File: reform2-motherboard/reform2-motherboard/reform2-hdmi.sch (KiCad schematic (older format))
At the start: 12 parts, among them J4 HDMI_A

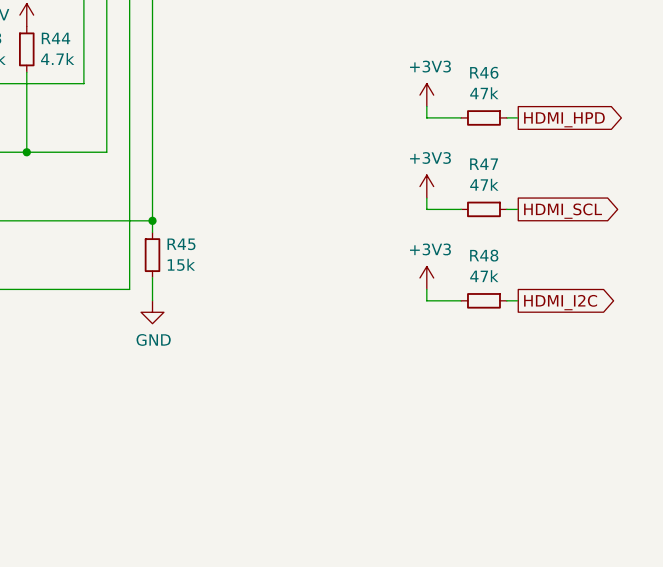
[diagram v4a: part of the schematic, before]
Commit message: WIP: reform2 motherboard: more schematics tuning, preliminary selection of most components
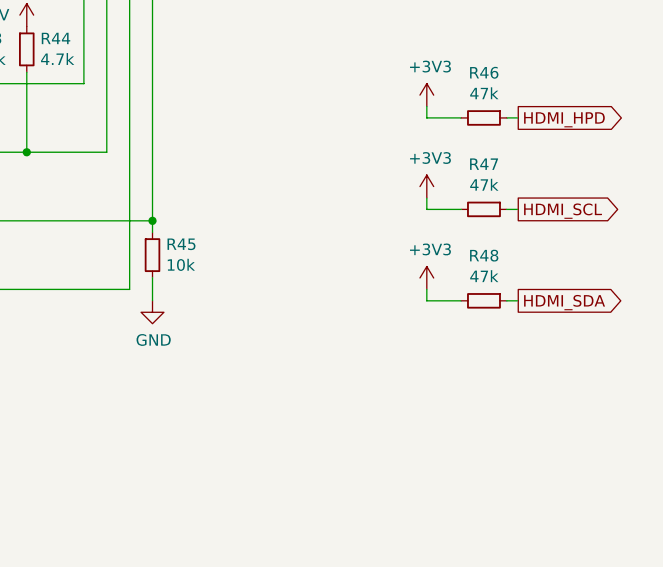
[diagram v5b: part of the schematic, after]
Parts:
- C27, C28, C29, C30: Manufacturer (none) -> TDK; Manufacturer_No (none) -> CGA3E2X8R1E104K080AE
- J4: Manufacturer (none) -> Wurth; Manufacturer_No (none) -> 685119134923
- R43, R44: Manufacturer (none) -> Yageo; Manufacturer_No (none) -> RC0603FR-074K7L
- R45: value 15k -> 10k; Manufacturer (none) -> Vishay Dale; Manufacturer_No (none) -> CRCW060310K0JNEAC
- R46, R47, R48: Manufacturer (none) -> Vishay Dale; Manufacturer_No (none) -> CRCW060347K0FKEAC
- U?1: Manufacturer (none) -> Texas Instruments; Manufacturer_No (none) -> CM2020-00TR
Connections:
- net HDMI_I2C is gone; now on net HDMI_SDA: R48.1
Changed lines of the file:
@@
 F 2 "footprints:HDMI-685119134923" H 8075 2600 50  0001 C CNN
 F 3 "https://en.wikipedia.org/wiki/HDMI" H 8075 2600 50  0001 C CNN
+F 4 "Wurth" H 8050 2600 50  0001 C CNN "Manufacturer"
+F 5 "685119134923" H 8050 2600 50  0001 C CNN "Manufacturer_No"
 	1    8050 2600
 	1    0    0    -1
@@
 F 4 "CM2020-00TR Series 10.8 V HDMI Transmitter Port Protection and Interface Device" H 3350 3150 50  0001 L BNN "Field6"
 F 5 "ON Semiconductor" H 4450 3050 50  0001 L BNN "Field8"
+F 6 "Texas Instruments" H 4800 5100 50  0001 C CNN "Manufacturer"
+F 7 "CM2020-00TR" H 4800 5100 50  0001 C CNN "Manufacturer_No"
 	1    4800 5100
 	1    0    0    -1
@@
 P 7550 5550
 F 0 "R45" H 7609 5596 50  0000 L CNN
-F 1 "15k" H 7609 5505 50  0000 L CNN
+F 1 "10k" H 7609 5505 50  0000 L CNN
 F 2 "Resistor_SMD:R_0603_1608Metric" H 7550 5550 50  0001 C CNN
 F 3 "~" H 7550 5550 50  0001 C CNN
+F 4 "Vishay Dale" H 7550 5550 50  0001 C CNN "Manufacturer"
+F 5 "CRCW060310K0JNEAC" H 7550 5550 50  0001 C CNN "Manufacturer_No"
 	1    7550 5550
 	1    0    0    -1
@@
 F 2 "Capacitor_SMD:C_0603_1608Metric" H 7400 1400 50  0001 C CNN
 F 3 "~" H 7400 1400 50  0001 C CNN
+F 4 "TDK" H 7400 1400 50  0001 C CNN "Manufacturer"
+F 5 "CGA3E2X8R1E104K080AE" H 7400 1400 50  0001 C CNN "Manufacturer_No"
 	1    7400 1400
 	1    0    0    -1
@@
 F 2 "Resistor_SMD:R_0603_1608Metric" H 6700 4650 50  0001 C CNN
 F 3 "~" H 6700 4650 50  0001 C CNN
+F 4 "Yageo" H 6700 4650 50  0001 C CNN "Manufacturer"
+F 5 "RC0603FR-074K7L" H 6700 4650 50  0001 C CNN "Manufacturer_No"
 	1    6700 4650
 	1    0    0    -1
@@
 F 2 "Resistor_SMD:R_0603_1608Metric" H 7000 4650 50  0001 C CNN
 F 3 "~" H 7000 4650 50  0001 C CNN
+F 4 "Yageo" H 7000 4650 50  0001 C CNN "Manufacturer"
+F 5 "RC0603FR-074K7L" H 7000 4650 50  0001 C CNN "Manufacturer_No"
 	1    7000 4650
 	1    0    0    -1
@@
 F 2 "Capacitor_SMD:C_0603_1608Metric" H 6800 4100 50  0001 C CNN
 F 3 "~" H 6800 4100 50  0001 C CNN
+F 4 "TDK" H 6800 4100 50  0001 C CNN "Manufacturer"
+F 5 "CGA3E2X8R1E104K080AE" H 6800 4100 50  0001 C CNN "Manufacturer_No"
 	1    6800 4100
 	0    -1   -1   0
@@
 F 2 "Capacitor_SMD:C_0603_1608Metric" H 6200 4000 50  0001 C CNN
 F 3 "~" H 6200 4000 50  0001 C CNN
+F 4 "TDK" H 6200 4000 50  0001 C CNN "Manufacturer"
+F 5 "CGA3E2X8R1E104K080AE" H 6200 4000 50  0001 C CNN "Manufacturer_No"
 	1    6200 4000
 	0    1    1    0
@@
 F 2 "Resistor_SMD:R_0603_1608Metric" H 9000 4950 50  0001 C CNN
 F 3 "~" H 9000 4950 50  0001 C CNN
+F 4 "Vishay Dale" H 9000 4950 50  0001 C CNN "Manufacturer"
+F 5 "CRCW060347K0FKEAC" H 9000 4950 50  0001 C CNN "Manufacturer_No"
 	1    9000 4950
 	0    1    1    0
@@
 F 2 "Capacitor_SMD:C_0603_1608Metric" H 6000 4500 50  0001 C CNN
 F 3 "~" H 6000 4500 50  0001 C CNN
+F 4 "TDK" H 6000 4500 50  0001 C CNN "Manufacturer"
+F 5 "CGA3E2X8R1E104K080AE" H 6000 4500 50  0001 C CNN "Manufacturer_No"
 	1    6000 4500
 	0    1    1    0
@@
 F 2 "Resistor_SMD:R_0603_1608Metric" H 9000 5350 50  0001 C CNN
 F 3 "~" H 9000 5350 50  0001 C CNN
+F 4 "Vishay Dale" H 9000 5350 50  0001 C CNN "Manufacturer"
+F 5 "CRCW060347K0FKEAC" H 9000 5350 50  0001 C CNN "Manufacturer_No"
 	1    9000 5350
 	0    1    1    0
@@
 	8750 5350 8750 5300
 Text GLabel 9150 5750 2    50   Output ~ 0
-HDMI_I2C
+HDMI_SDA
 $Comp
 L power:+3V3 #PWR0169
@@
 F 2 "Resistor_SMD:R_0603_1608Metric" H 9000 5750 50  0001 C CNN
 F 3 "~" H 9000 5750 50  0001 C CNN
+F 4 "Vishay Dale" H 9000 5750 50  0001 C CNN "Manufacturer"
+F 5 "CRCW060347K0FKEAC" H 9000 5750 50  0001 C CNN "Manufacturer_No"
 	1    9000 5750
 	0    1    1    0

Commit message: WIP: reform2 motherboard: rough placement
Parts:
- renumbered U?1 to U22
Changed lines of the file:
@@
 HDMI_D0+
 $Comp
-L reform2:CM2020-00TR U?1
+L reform2:CM2020-00TR U22
 U 1 1 5D124B0E
 P 4800 5100
-F 0 "U?1" H 4800 6467 50  0000 C CNN
+F 0 "U22" H 4800 6467 50  0000 C CNN
 F 1 "CM2020-00TR" H 4800 6376 50  0000 C CNN
 F 2 "footprints:TSSOP50P640X120-38N" H 4350 2950 50  0001 L BNN
